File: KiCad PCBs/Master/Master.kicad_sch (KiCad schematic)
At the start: 17 parts

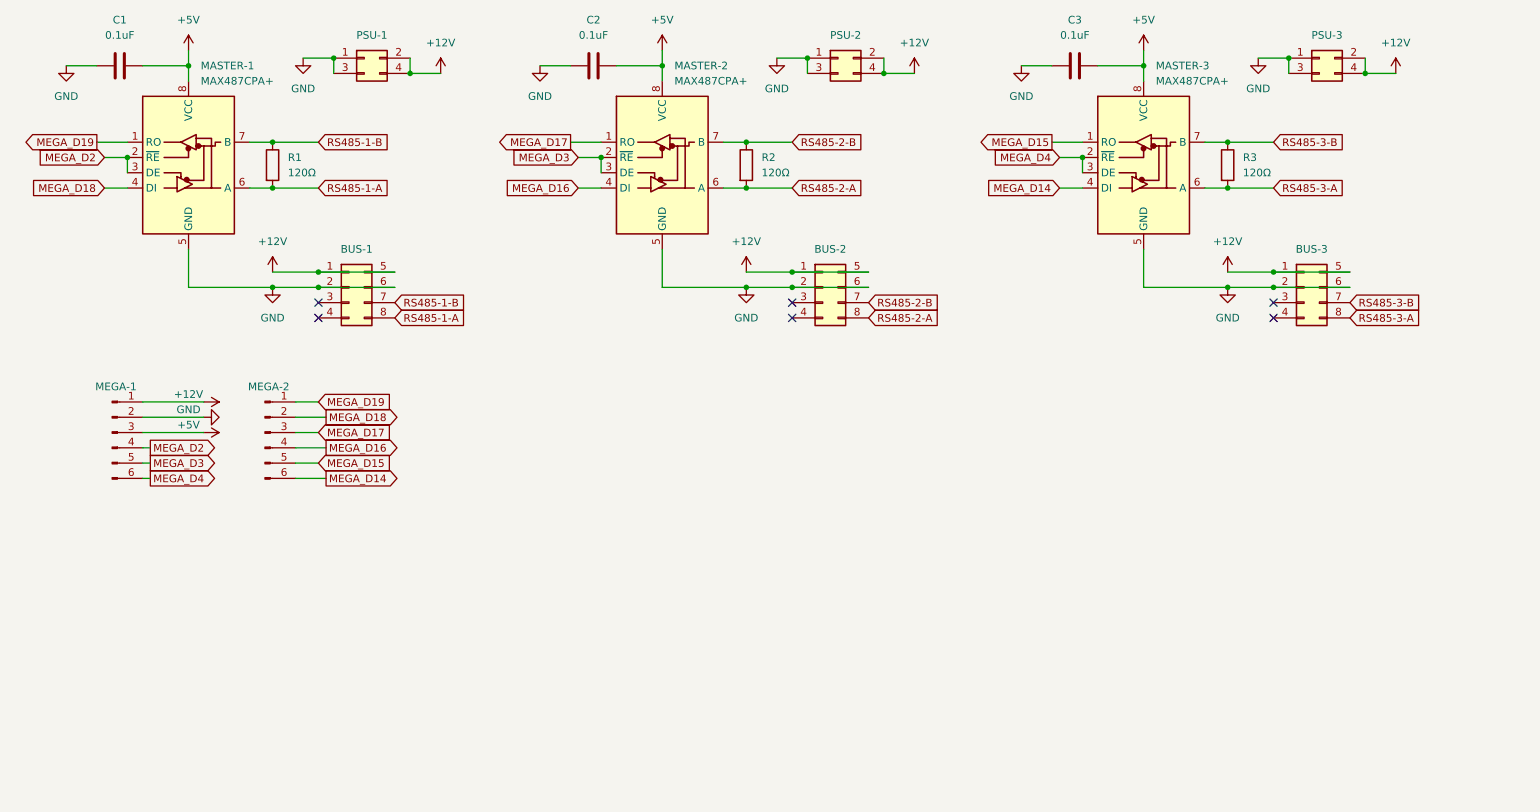
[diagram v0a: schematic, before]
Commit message: Added Micro Blade fuse holder to each bus Updated cap 3d model Ignored KiCad backups
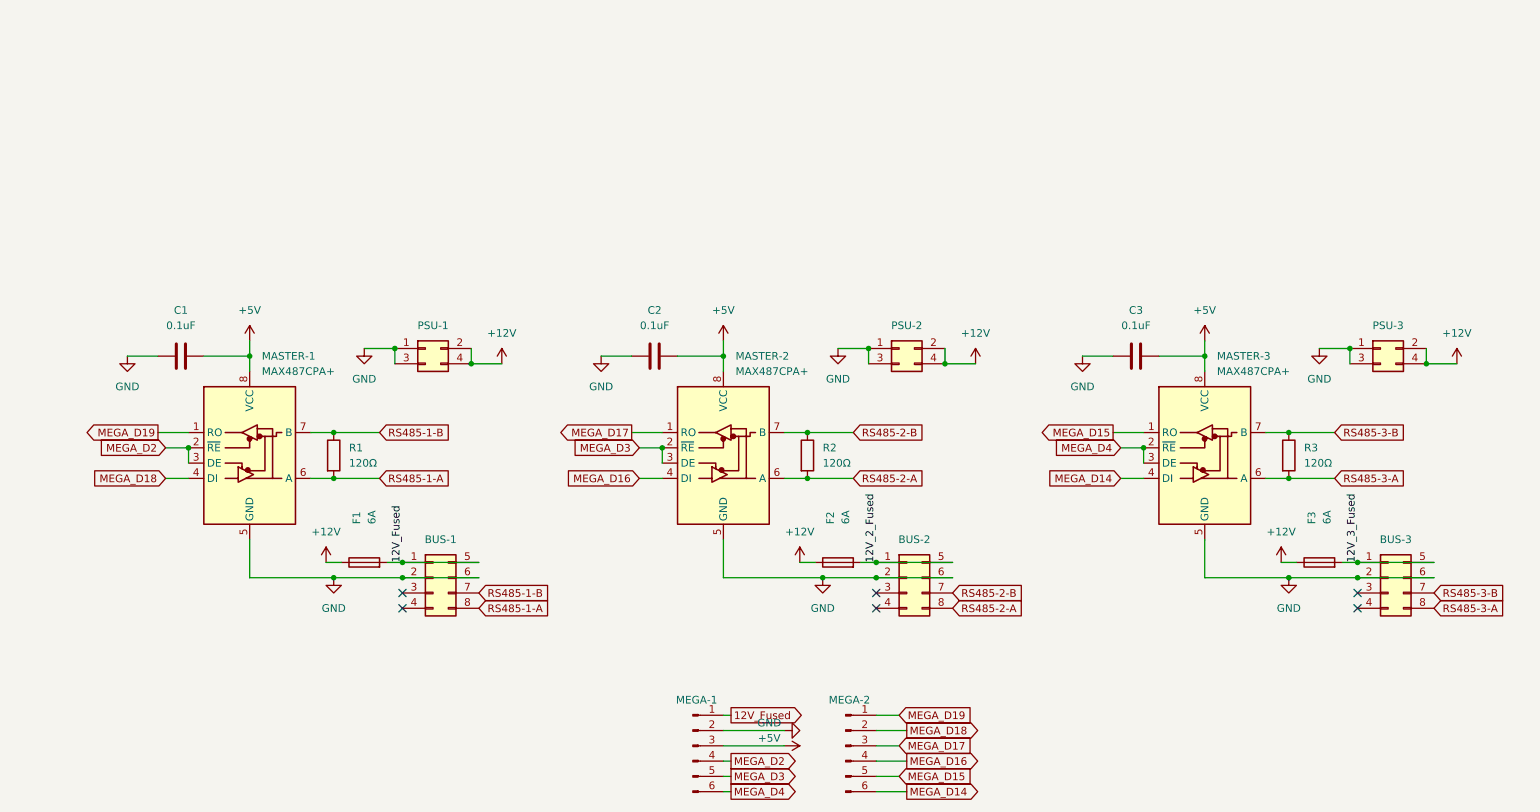
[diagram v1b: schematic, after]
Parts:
- added F1, F2, F3: 6A, A10 KiCad Libraries:FUSE_BK-6013, symbol Device:Fuse
- C1, C2, C3: footprint Capacitor_THT:C_Disc_D5.0mm_W2.5mm_P2.50mm -> A10 KiCad Libraries:FA14
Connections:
- net +12V: now also F1.1; no longer BUS-1.1 (Pin_1), BUS-1.5 (Pin_5), MEGA-1.1 (Pin_1)
- net +12V_2: now also F2.1; no longer BUS-2.1 (Pin_1), BUS-2.5 (Pin_5)
- net +12V_3: now also F3.1; no longer BUS-3.1 (Pin_1), BUS-3.5 (Pin_5)
- new net 12V_2_Fused: BUS-2.1 (Pin_1), BUS-2.5 (Pin_5), F2.2
- new net 12V_3_Fused: BUS-3.1 (Pin_1), BUS-3.5 (Pin_5), F3.2
- new net 12V_Fused: BUS-1.1 (Pin_1), BUS-1.5 (Pin_5), F1.2, MEGA-1.1 (Pin_1)
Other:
- moved on the sheet: BUS-1, BUS-2, BUS-3, C1, C2, C3, MASTER-1, MASTER-2, MASTER-3, MEGA-1, MEGA-2, PSU-1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

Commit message: Added power status LEDs to Master PCB
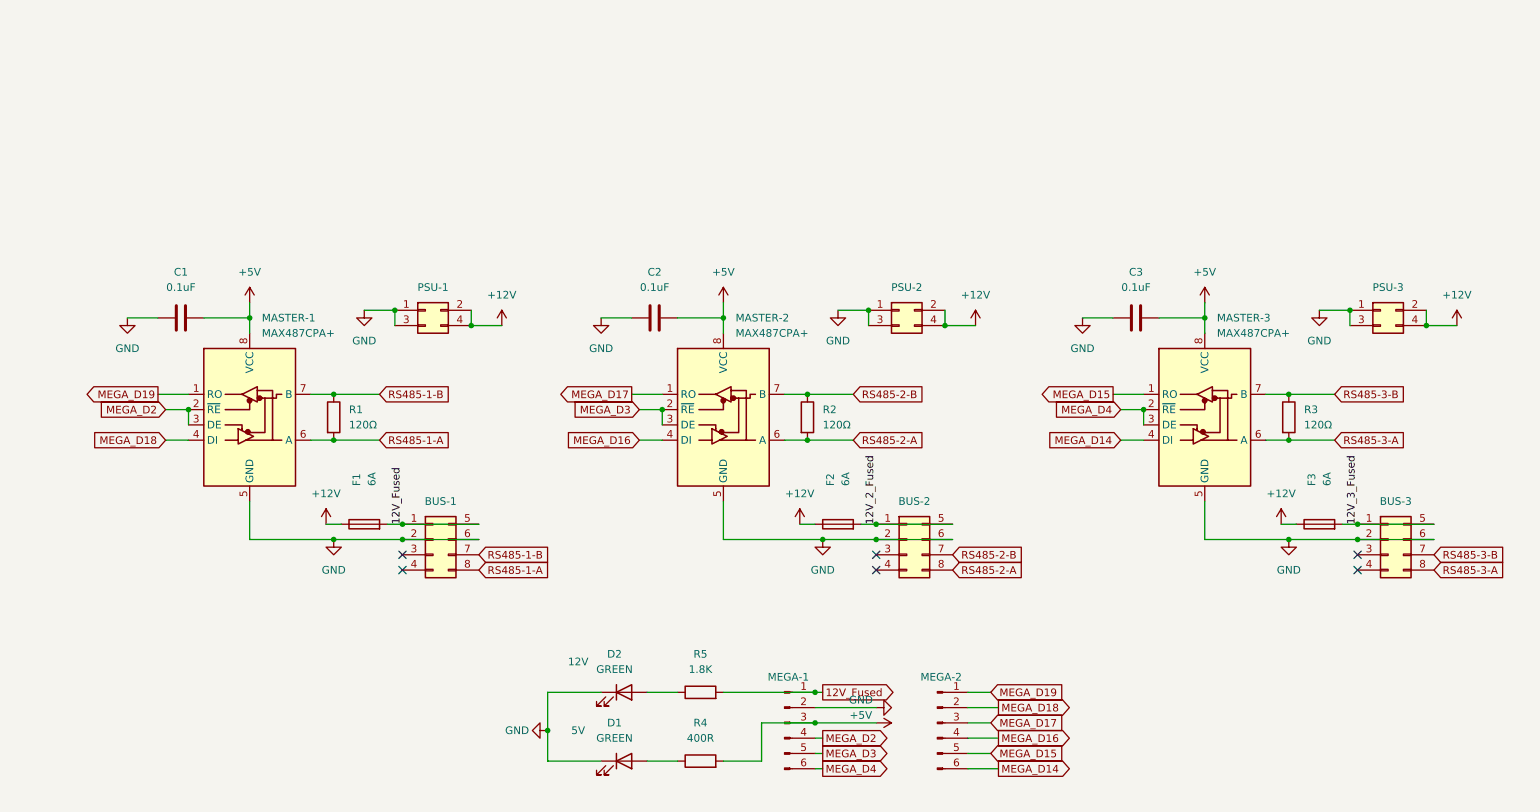
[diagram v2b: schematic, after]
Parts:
- added D1, D2: GREEN, LED_SMD:LED_1210_3225Metric_Pad1.42x2.65mm_HandSolder, symbol Device:LED
- added R4: 400R, Resistor_SMD:R_1210_3225Metric_Pad1.30x2.65mm_HandSolder, symbol Device:R
- added R5: 1.8K, Resistor_SMD:R_1210_3225Metric_Pad1.30x2.65mm_HandSolder, symbol Device:R
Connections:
- net +5V: now also R4.2
- net 12V_Fused: now also R5.2
- net GND: now also D1.1 (K), D2.1 (K)
- new net: D1.2 (A), R4.1
- new net: D2.2 (A), R5.1
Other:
- moved on the sheet: BUS-1, BUS-2, BUS-3, C1, C2, C3, F1, F2, F3, MASTER-1, MASTER-2, MASTER-3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

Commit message: Added power status LED to each bus
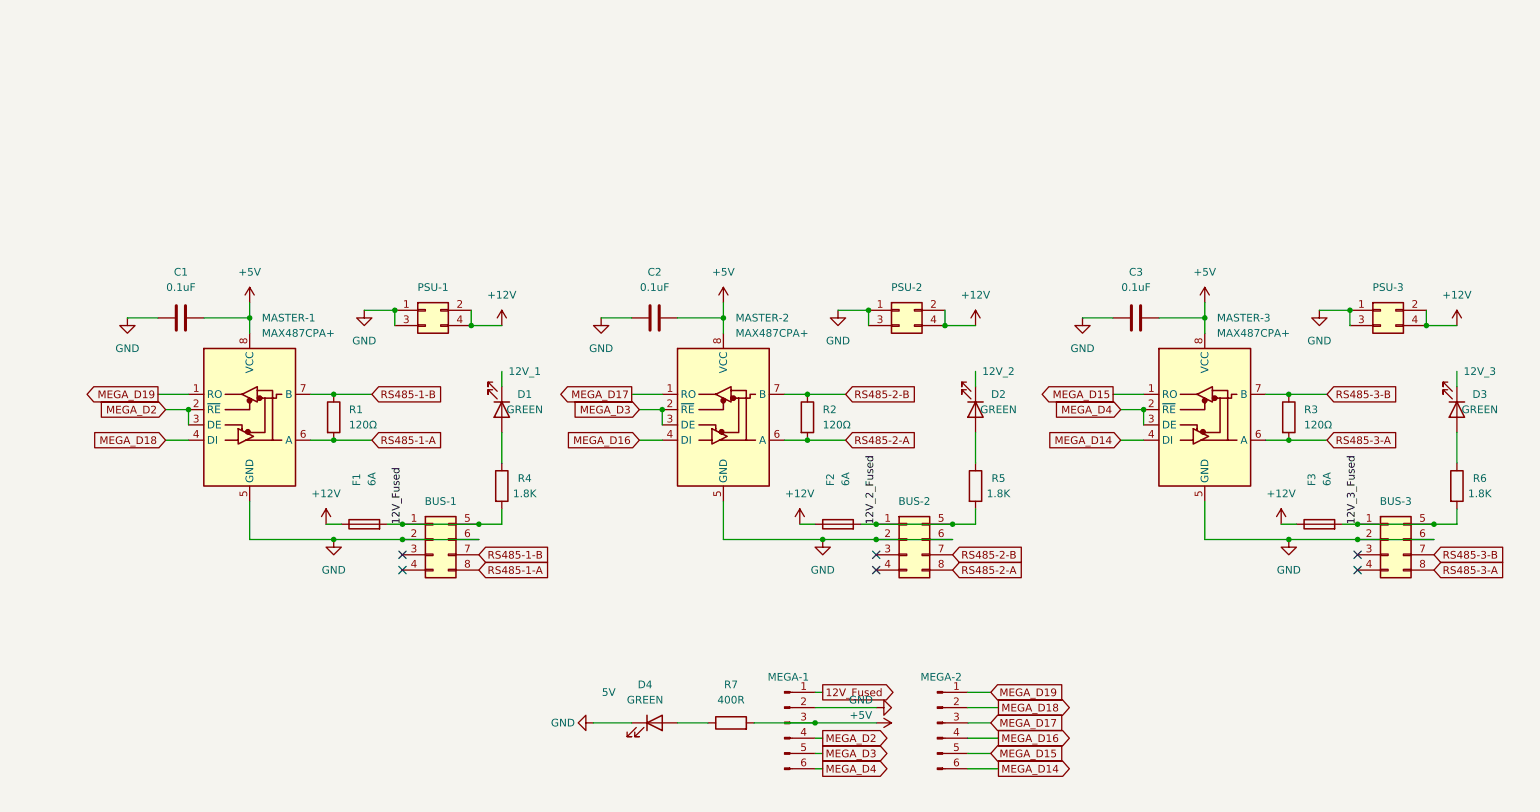
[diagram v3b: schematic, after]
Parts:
- added D1, D3: GREEN, LED_SMD:LED_1210_3225Metric_Pad1.42x2.65mm_HandSolder, symbol Device:LED
- added R4, R6: 1.8K, Resistor_SMD:R_1210_3225Metric_Pad1.30x2.65mm_HandSolder, symbol Device:R
- D2: Field4 12V -> 12V_2
- renumbered D1 to D4, R4 to R7
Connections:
- net 12V_2_Fused: now also R5.2
- net 12V_3_Fused: now also R6.2
- net 12V_Fused: now also R4.2; no longer R5.2
- net GND: no longer D2.1 (K)
- new net: D3.2 (A), R6.1
- new net: D1.2 (A), R4.1
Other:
- moved on the sheet: D4, R7

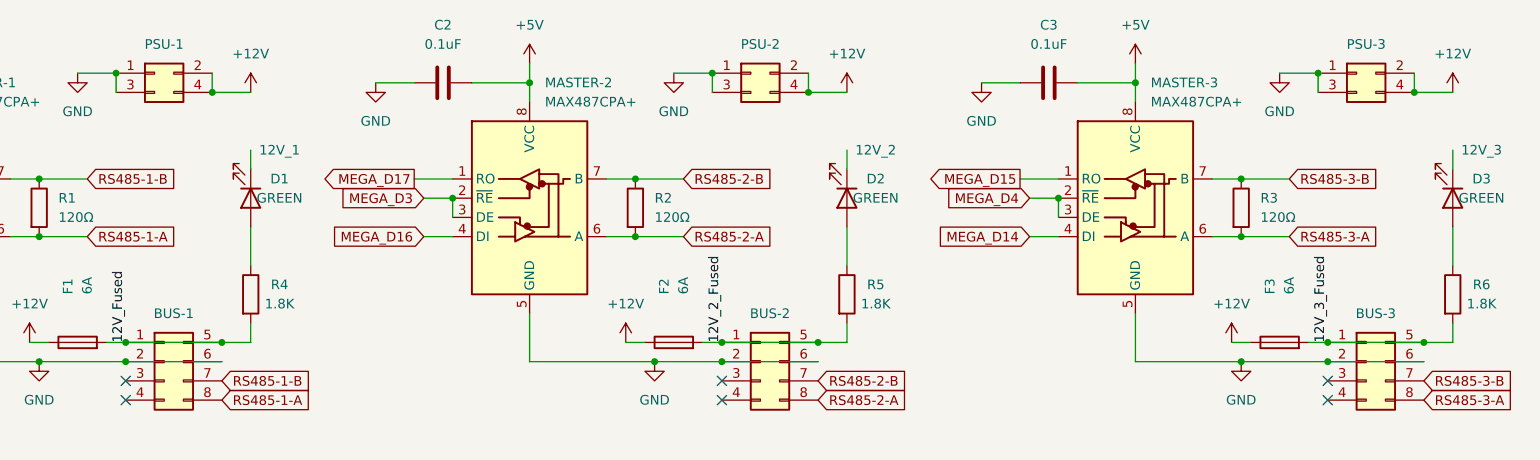
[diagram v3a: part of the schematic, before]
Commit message: Updated Master PCB and completed first version of Hub
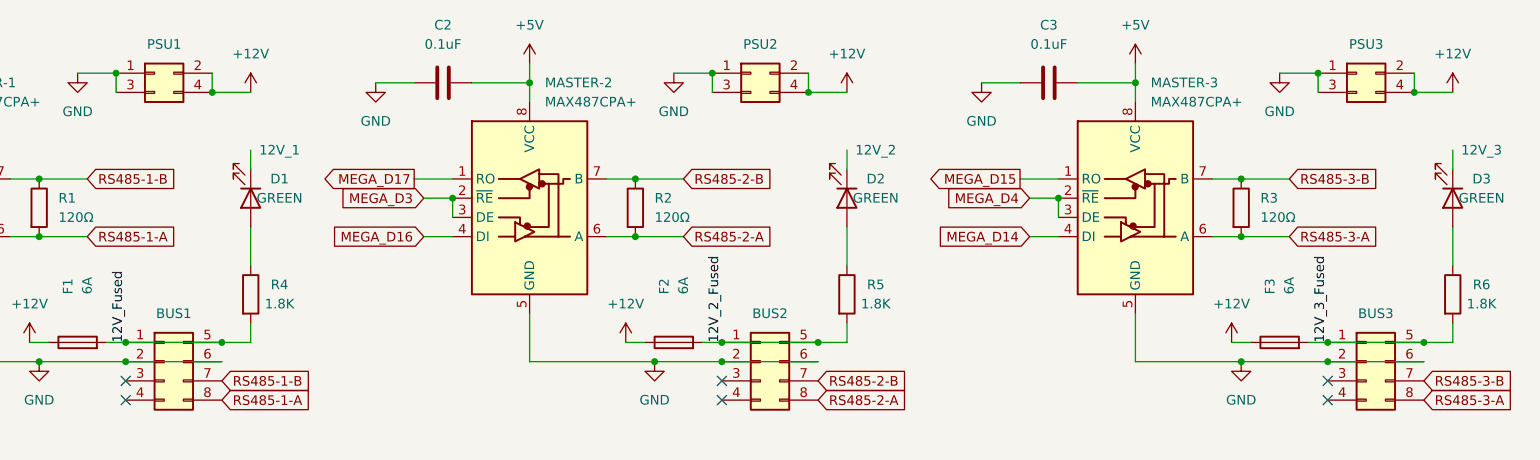
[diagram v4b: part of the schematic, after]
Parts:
- BUS1: renamed from BUS-1; LCSC (none) -> C122422
- renumbered BUS-2 to BUS2, BUS-3 to BUS3, PSU-1 to PSU1, PSU-2 to PSU2, PSU-3 to PSU3
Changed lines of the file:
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@@
   (symbol (lib_id "Connector_Generic:Conn_02x02_Odd_Even") (at 162.56 68.58 0) (unit 1)
     (in_bom yes) (on_board yes) (fields_autoplaced)
-    (property "Reference" "PSU-2" (id 0) (at 163.83 64.77 0))
+    (property "Reference" "PSU2" (id 0) (at 163.83 64.77 0))
     (property "Value" "Conn_02x02_Top_Bottom" (id 1) (at 163.83 64.77 0)
       (effects (font (size 1.27 1.27)) hide)
@@
   (symbol (lib_id "Connector_Generic:Conn_02x04_Top_Bottom") (at 243.84 106.68 0) (unit 1)
     (in_bom yes) (on_board yes) (fields_autoplaced)
-    (property "Reference" "BUS-3" (id 0) (at 245.11 100.33 0))
+    (property "Reference" "BUS3" (id 0) (at 245.11 100.33 0))
     (property "Value" "Conn_02x04_Top_Bottom" (id 1) (at 245.11 100.33 0)
       (effects (font (size 1.27 1.27)) hide)
@@
   (symbol (lib_id "Connector_Generic:Conn_02x02_Odd_Even") (at 83.82 68.58 0) (unit 1)
     (in_bom yes) (on_board yes)
-    (property "Reference" "PSU-1" (id 0) (at 85.09 64.77 0))
+    (property "Reference" "PSU1" (id 0) (at 85.09 64.77 0))
     (property "Value" "Conn_02x02_Top_Bottom" (id 1) (at 85.09 64.77 0)
       (effects (font (size 1.27 1.27)) hide)
@@
   (symbol (lib_id "Connector_Generic:Conn_02x04_Top_Bottom") (at 85.09 106.68 0) (unit 1)
     (in_bom yes) (on_board yes)
-    (property "Reference" "BUS-1" (id 0) (at 86.36 100.33 0))
+    (property "Reference" "BUS1" (id 0) (at 86.36 100.33 0))
     (property "Value" "Conn_02x04_Top_Bottom" (id 1) (at 86.36 100.33 0)
       (effects (font (size 1.27 1.27)) hide)
@@
     )
     (property "Datasheet" "~" (id 3) (at 85.09 106.68 0)
+      (effects (font (size 1.27 1.27)) hide)
+    )
+    (property "LCSC" "C122422" (id 4) (at 85.09 106.68 0)
       (effects (font (size 1.27 1.27)) hide)
     )
@@
   (symbol (lib_id "Connector_Generic:Conn_02x02_Odd_Even") (at 242.57 68.58 0) (unit 1)
     (in_bom yes) (on_board yes) (fields_autoplaced)
-    (property "Reference" "PSU-3" (id 0) (at 243.84 64.77 0))
+    (property "Reference" "PSU3" (id 0) (at 243.84 64.77 0))
     (property "Value" "Conn_02x02_Top_Bottom" (id 1) (at 243.84 64.77 0)
       (effects (font (size 1.27 1.27)) hide)
@@
   (symbol (lib_id "Connector_Generic:Conn_02x04_Top_Bottom") (at 163.83 106.68 0) (unit 1)
     (in_bom yes) (on_board yes) (fields_autoplaced)
-    (property "Reference" "BUS-2" (id 0) (at 165.1 100.33 0))
+    (property "Reference" "BUS2" (id 0) (at 165.1 100.33 0))
     (property "Value" "Conn_02x04_Top_Bottom" (id 1) (at 165.1 100.33 0)
       (effects (font (size 1.27 1.27)) hide)
@@
     )
     (path "/a75f5aaa-0001-416b-b014-9e6ac6c531e2"
-      (reference "BUS-1") (unit 1) (value "Conn_02x04_Top_Bottom") (footprint "A10 KiCad Libraries:Molex 43045-0800")
+      (reference "BUS1") (unit 1) (value "Conn_02x04_Top_Bottom") (footprint "A10 KiCad Libraries:Molex 43045-0800")
     )
     (path "/f14a865a-0c1a-4718-b8aa-20f98e1fb05b"
-      (reference "BUS-2") (unit 1) (value "Conn_02x04_Top_Bottom") (footprint "A10 KiCad Libraries:Molex 43045-0800")
+      (reference "BUS2") (unit 1) (value "Conn_02x04_Top_Bottom") (footprint "A10 KiCad Libraries:Molex 43045-0800")
     )
     (path "/738559db-5500-4ab5-924e-ba6720bbcddb"
-      (reference "BUS-3") (unit 1) (value "Conn_02x04_Top_Bottom") (footprint "A10 KiCad Libraries:Molex 43045-0800")
+      (reference "BUS3") (unit 1) (value "Conn_02x04_Top_Bottom") (footprint "A10 KiCad Libraries:Molex 43045-0800")
     )
     (path "/3a769895-08d0-40ba-b6f4-0e1eab77a19d"
@@
     )
     (path "/8aeff167-f265-4578-8cff-576a3c644747"
-      (reference "PSU-1") (unit 1) (value "Conn_02x02_Top_Bottom") (footprint "A10 KiCad Libraries:Molex 43045-0400")
+      (reference "PSU1") (unit 1) (value "Conn_02x02_Top_Bottom") (footprint "A10 KiCad Libraries:Molex 43045-0400")
     )
     (path "/46e746c8-c244-4ddb-9dd9-13de65377d91"
-      (reference "PSU-2") (unit 1) (value "Conn_02x02_Top_Bottom") (footprint "A10 KiCad Libraries:Molex 43045-0400")
+      (reference "PSU2") (unit 1) (value "Conn_02x02_Top_Bottom") (footprint "A10 KiCad Libraries:Molex 43045-0400")
     )
     (path "/c3ba1114-ad95-4b4b-9b5c-011231b74217"
-      (reference "PSU-3") (unit 1) (value "Conn_02x02_Top_Bottom") (footprint "A10 KiCad Libraries:Molex 43045-0400")
+      (reference "PSU3") (unit 1) (value "Conn_02x02_Top_Bottom") (footprint "A10 KiCad Libraries:Molex 43045-0400")
     )
     (path "/a711285c-9b66-40e7-8c5e-7252c7ffcdb9"
